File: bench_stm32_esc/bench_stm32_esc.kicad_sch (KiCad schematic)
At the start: 107 parts, among them CN1 S6B-PH-K-S-, CN10 Conn_02x19_Odd_Even, CN7 Conn_02x19_Odd_Even, J1 XT60PW-M, Q1 CSD19532Q5B, Q2 CSD19532Q5B, Q3 CSD19532Q5B, Q4 CSD19532Q5B, Q5 CSD19532Q5B, Q6 CSD19532Q5B, U1 DRV8353RSRGZT, U2 AMS1117, U3 TPD1E05U06DYA, U4 MR60PW-M.G.B, U7 TB60

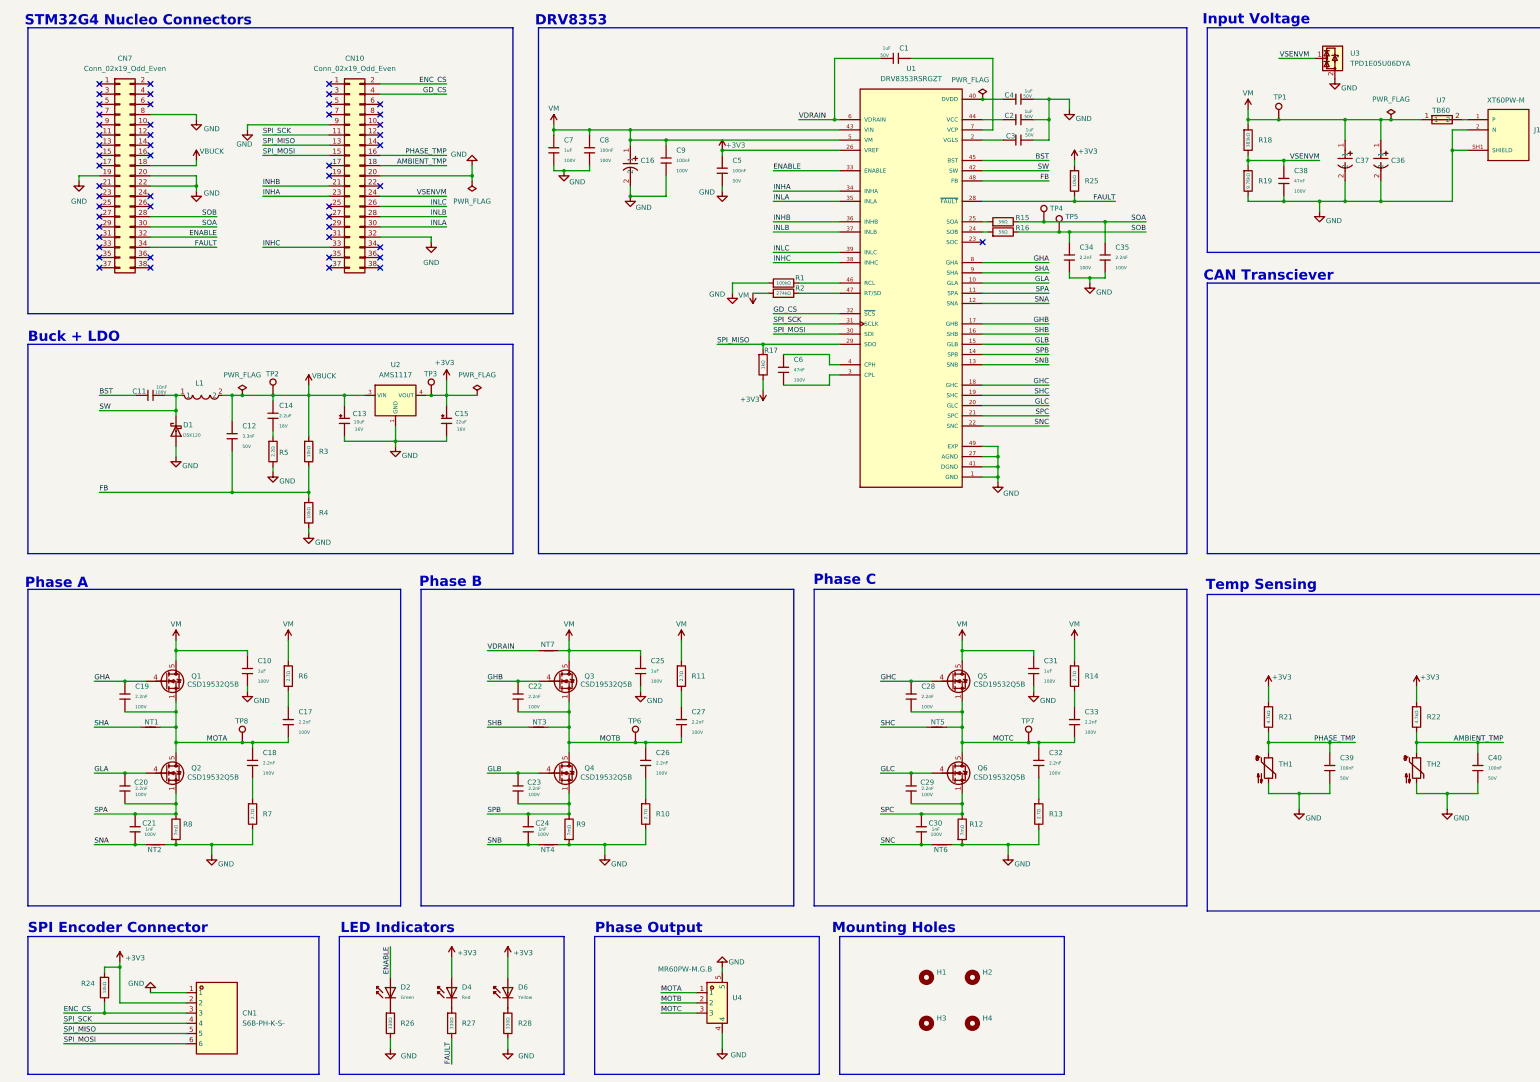
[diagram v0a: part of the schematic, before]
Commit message: Added smd stm32
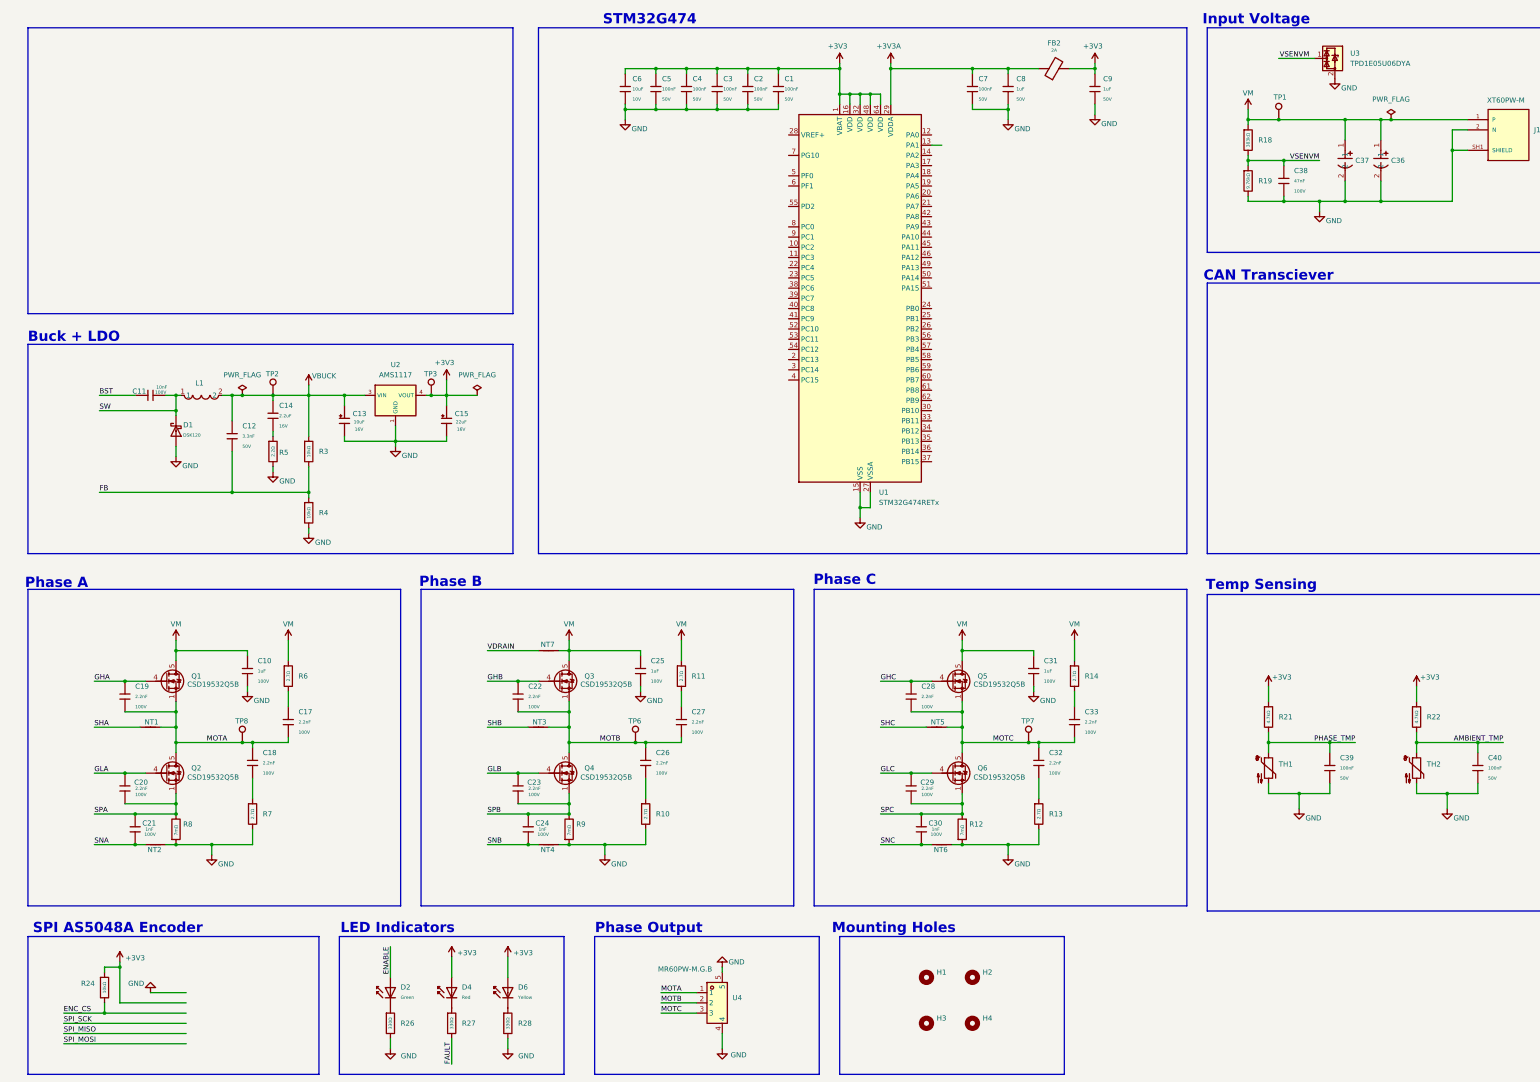
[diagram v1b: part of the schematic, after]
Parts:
- removed C1, C2, C3, C4: 1uF, PCM_JLCPCB:C_0603, symbol PCM_JLCPCB-Capacitors:0603,1uF
- removed C16: VT10UF100V167RV0127, footprints:VT10UF100V167RV0127, symbol VT10UF100V167RV0127:VT10UF100V167RV0127
- removed C34, C35: 2.2nF, PCM_JLCPCB:C_0603, symbol PCM_JLCPCB-Capacitors:0603,2.2uF
- removed C6: 47nF, PCM_JLCPCB:C_0603, symbol PCM_JLCPCB-Capacitors:0603,47nF
- removed C7: 1uF, PCM_JLCPCB:C_0805, symbol PCM_JLCPCB-Capacitors:0805,1uF
- removed C8, C9: 100nF, PCM_JLCPCB:C_0603, symbol PCM_JLCPCB-Capacitors:0603,100nF
- removed CN1: S6B-PH-K-S-, footprints:S6B-PH-K-S(LF)(SN), symbol S6B-PH-K-S(LF)(SN):S6B-PH-K-S-
- removed CN10, CN7: Conn_02x19_Odd_Even, Connector_PinSocket_2.54mm:PinSocket_2x19_P2.54mm_Vertical, symbol Connector_Generic:Conn_02x19_Odd_Even
- removed R1: 100kΩ, PCM_JLCPCB:R_0603, symbol PCM_JLCPCB-Resistors:0603,100kΩ
- removed R15, R16: 56Ω, PCM_JLCPCB:R_0603, symbol PCM_JLCPCB-Resistors:0603,56Ω
- removed R17: 1kΩ, PCM_JLCPCB:R_0603, symbol PCM_JLCPCB-Resistors:0603,1kΩ
- removed R2: 274kΩ, PCM_JLCPCB:R_0603, symbol PCM_JLCPCB-Resistors:0603,100kΩ
- removed R25: 10kΩ, PCM_JLCPCB:R_0603, symbol PCM_JLCPCB-Resistors:0603,10kΩ
- removed TP4, TP5: TestPoint, TestPoint:TestPoint_Pad_1.5x1.5mm, symbol Connector:TestPoint
- removed U1: DRV8353RSRGZT, footprints:QFN50P700X700X100-49N, symbol DRV8353RSRGZT:DRV8353RSRGZT
- removed U7: TB60, footprints:TB60, symbol TB60:TB60
- added C1, C2, C3, C4, C7: 100nF, PCM_JLCPCB:C_0603, symbol PCM_JLCPCB-Capacitors:0603,100nF
- added C6: 10uF, PCM_JLCPCB:C_0603, symbol PCM_JLCPCB-Capacitors:0603,10uF
- added C8, C9: 1uF, PCM_JLCPCB:C_0603, symbol PCM_JLCPCB-Capacitors:0603,1uF
- added FB2: (no value), PCM_JLCPCB:FB_0603, symbol PCM_JLCPCB-Inductors:Ferrite,0603,(2)
- added U1: STM32G474RETx, Package_QFP:LQFP-64_10x10mm_P0.5mm, symbol MCU_ST_STM32G4:STM32G474RETx
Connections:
- net +3V3: now also C1.1, C2.1, C3.1, C4.1, C6.2, C9.1, FB2.2, U1.1 (VBAT), U1.16 (VDD), U1.32 (VDD), U1.48 (VDD), U1.64 (VDD)
- net GND: now also C1.2, C2.2, C3.2, C4.2, C6.1, C7.2, C8.2, C9.2, U1.15 (VSS), U1.27 (VSSA), U1.31 (VSS), U1.47 (VSS), U1.63 (VSS)
- net VM: now also J1.1 (P)
- new net +3V3A: C7.1, C8.1, FB2.1, U1.29 (VDDA)
- no-connect marks 51 -> 0
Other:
- note added: "SPI AS5048A Encoder"
- note added: "STM32G474"
- note removed: "DRV8353"
- note removed: "SPI Encoder Connector"
- note removed: "STM32G4 Nucleo Connectors"

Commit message: New gate drivers
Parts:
- removed C11: 10nF, PCM_JLCPCB:C_0603, symbol PCM_JLCPCB-Capacitors:0603,100nF
- removed C12: 3.3nF, PCM_JLCPCB:C_0603, symbol PCM_JLCPCB-Capacitors:0603,3.3nF
- removed C13: 10uF, PCM_JLCPCB:C_CASE-A-3216-18(mm), symbol PCM_JLCPCB-Capacitors:CASE-A-3216-18(mm),10uF
- removed C14: 2.2uF, PCM_JLCPCB:C_0603, symbol PCM_JLCPCB-Capacitors:0603,2.2uF
- removed C15: 22uF, PCM_JLCPCB:C_CASE-A-3216-18(mm), symbol PCM_JLCPCB-Capacitors:CASE-A-3216-18(mm),10uF
- removed C17, C18, C22, C23, C26, C27, C28, C29, C32, C33: 2.2nF, PCM_JLCPCB:C_0603, symbol PCM_JLCPCB-Capacitors:0603,2.2uF
- removed C21, C24, C30: 1nF, PCM_JLCPCB:C_0603, symbol PCM_JLCPCB-Capacitors:0603,1nF
- removed C25, C31: 1uF, PCM_JLCPCB:C_0805, symbol PCM_JLCPCB-Capacitors:0805,1uF
- removed D1: DSK120, PCM_JLCPCB:D_SOD-123FL, symbol PCM_JLCPCB-Diodes:Schottky,DSK120
- removed D4: Red, PCM_JLCPCB:D_0805, symbol PCM_JLCPCB-Diodes:LED,0805,Red
- removed H4: MountingHole, MountingHole:MountingHole_3.2mm_M3, symbol Mechanical:MountingHole
- removed L1: SMDRH104R-331MT, footprints:SMDRH104R-331MT, symbol SMDRH104R-331MT:SMDRH104R-331MT
- removed NT1, NT2, NT3, NT4, NT5, NT6: NetTie_2, NetTie:NetTie-2_SMD_Pad0.5mm, symbol Device:NetTie_2
- removed NT7: NetTie_2, NetTie:NetTie-2_SMD_Pad2.0mm, symbol Device:NetTie_2
- removed Q3, Q4, Q5, Q6: CSD19532Q5B, Package_TO_SOT_SMD:TDSON-8-1, symbol Transistor_FET:CSD19532Q5B
- removed R10, R11, R13, R14, R6, R7: 2.7Ω, PCM_JLCPCB:R_0805, symbol PCM_JLCPCB-Resistors:0805,2.2Ω
- removed R12, R8, R9: 7mΩ, Resistor_SMD:R_2512_6332Metric, symbol Device:R
- removed R24, R3, R4: 10kΩ, PCM_JLCPCB:R_0603, symbol PCM_JLCPCB-Resistors:0603,10kΩ
- removed R27: 330Ω, PCM_JLCPCB:R_0603, symbol PCM_JLCPCB-Resistors:0603,330Ω
- removed R5: 2.2Ω, PCM_JLCPCB:R_0603, symbol PCM_JLCPCB-Resistors:0603,2.2Ω
- removed TP2, TP3, TP6, TP7: TestPoint, TestPoint:TestPoint_Pad_1.5x1.5mm, symbol Connector:TestPoint
- removed U2: AMS1117, PCM_JLCPCB:SOT-223-3_L6.5-W3.4-P2.30-LS7.0-BR, symbol PCM_JLCPCB-Power:LDO, 3.3V, 1A
- added C1, C4: 10pF, PCM_JLCPCB:C_0603, symbol PCM_JLCPCB-Capacitors:0603,10pF
- added C11, C12: 2.2nF, PCM_JLCPCB:C_0603, symbol PCM_JLCPCB-Capacitors:0603,2.2uF
- added C13, C19, C23, C28, C3, C5: 100nF, PCM_JLCPCB:C_0603, symbol PCM_JLCPCB-Capacitors:0603,100nF
- added C2, C25, C37, C42: 2.2uF, PCM_JLCPCB:C_0603, symbol PCM_JLCPCB-Capacitors:0603,2.2uF
- added C26, C6: 1uF, PCM_JLCPCB:C_0603, symbol PCM_JLCPCB-Capacitors:0603,1uF
- added C31, C36: 2.2nF, PCM_JLCPCB:C_0603, symbol PCM_JLCPCB-Capacitors:0603,2.2nF
- added C34: 58pF, PCM_JLCPCB:C_0603, symbol PCM_JLCPCB-Capacitors:0603,33pF
- added C39, C41, C44: 22uF, PCM_JLCPCB:C_0603, symbol PCM_JLCPCB-Capacitors:0603,22uF
- added FB1: (no value), PCM_JLCPCB:FB_0603, symbol PCM_JLCPCB-Inductors:Ferrite,0603
- added J1: USB_C_Receptacle_USB2.0_16P, Connector_USB:USB_C_Receptacle_HRO_TYPE-C-31-M-12, symbol Connector:USB_C_Receptacle_USB2.0_16P
- added L2: SM7850-680MT, footprints:SM7850-680MT, symbol SM7850-680MT:SM7850-680MT
- added R1, R3: 3.3Ω, PCM_JLCPCB:R_0603, symbol PCM_JLCPCB-Resistors:0603,4.7Ω
- added R10: 100kΩ, PCM_JLCPCB:R_0603, symbol PCM_JLCPCB-Resistors:0603,100kΩ
- added R13, R6: 10kΩ, PCM_JLCPCB:R_0603, symbol PCM_JLCPCB-Resistors:0603,10kΩ
- added R15: 150kΩ, PCM_JLCPCB:R_0603, symbol PCM_JLCPCB-Resistors:0603,150kΩ
- added R16, R17: 5.1kΩ, PCM_JLCPCB:R_0603, symbol PCM_JLCPCB-Resistors:0603,5.1kΩ
- added R19: 360kΩ, PCM_JLCPCB:R_0603, symbol PCM_JLCPCB-Resistors:0603,360kΩ
- added R21: 470kΩ, PCM_JLCPCB:R_0603, symbol PCM_JLCPCB-Resistors:0603,470kΩ
- added R4, R5: 2.7Ω, PCM_JLCPCB:R_0805, symbol PCM_JLCPCB-Resistors:0805,2.2Ω
- added R8: 330kΩ, PCM_JLCPCB:R_0603, symbol PCM_JLCPCB-Resistors:0603,330kΩ
- added SW1: SW_SPDT, symbol Switch:SW_SPDT
- added U1: UCC27211ADRMR, easyeda2kicad:VSON-8_L4.0-W4.0-P0.80-TL-EP, symbol easyeda2kicad:UCC27211ADRMR
- added U10: AS5047D, Package_SO:TSSOP-14_4.4x5mm_P0.65mm, symbol Sensor_Magnetic:AS5047D
- added U11: USBLC6-2P6, Package_TO_SOT_SMD:SOT-666, symbol Power_Protection:USBLC6-2P6
- added U4: AP2112K-3.3, Package_TO_SOT_SMD:SOT-23-5, symbol Regulator_Linear:AP2112K-3.3
- added U5: INA240A2D, Package_SO:SOIC-8_3.9x4.9mm_P1.27mm, symbol Amplifier_Current:INA240A2D
- added U8: LM5164DDA, Package_SO:HSOP-8-1EP_3.9x4.9mm_P1.27mm_EP2.41x3.1mm_ThermalVias, symbol Regulator_Switching:LM5164DDA
- added X1: X322516MLB4SI, PCM_JLCPCB:OSC-SMD_4P-L3.2-W2.5-BL, symbol PCM_JLCPCB-Crystals:Crystal, 16MHz, 9pF
- renumbered C6 to C14, C5 to C15, C4 to C16, C3 to C17, C2 to C18, C1 to C20, C7 to C21, C8 to C22, C38 to C27, C37 to C29, C36 to C32, C39 to C45, C40 to C46, C19 to C7, C20 to C8, D2 to D1, D6 to D2, H3 to H2, H2 to H3, J1 to J2, R18 to R11, R19 to R12, R26 to R22, R28 to R23, R21 to R24, R22 to R25, TP8 to TP1, TP1 to TP2, U4 to U12, U1 to U6, U3 to U9
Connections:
- net AMBIENT_TMP is gone; now on net AMB_TMP: C46.1, R25.2, TH2.1
- net SPA is gone; now on net GND: C8.2, Q2.1 (S), Q2.2 (S), Q2.3 (S)
- net +3V3: now also C19.1, C23.1, C26.1, C28.1, FB1.2, R13.1, SW1.3 (C), U10.11 (VDD), U4.5 (VOUT), U5.3 (REF2), U5.6 (V+); no longer FB2.2
- net +3V3A: now also FB1.1; no longer FB2.1
- net GHA: now also R3.2
- net GLA: now also R1.1
- net GND: now also C1.2, C13.2, C19.2, C2.2, C23.2, C25.2, C26.2, C28.2, C3.2, C37.2, C39.2, C4.2, C41.2, C42.2, C44.2, C6.2, J1.A1 (GND), J1.A12 (GND), J1.B1 (GND), J1.B12 (GND), J1.SH (SHIELD), R10.2, R15.2, R16.1, R17.1, R5.2, R8.2, SW1.1 (A), U1.7 (VSS), U1.9 (EP), U10.13 (GND), U10.5 (TST), U11.2 (GND), U4.2 (GND), U5.2 (GND), U5.4 (GND), U5.7 (REF1), U8.1 (GND), U8.9 (EP), X1.2 (GND), X1.4 (GND)
- net MOTA: now also U5.8 (+); no longer C7.2, Q1.1 (S), Q1.2 (S), Q1.3 (S), Q2.5 (D), TP1.1
- net PHASE_TMP: now also U6.13 (PA1)
- net SPI_MISO: now also U6.53 (PC11)
- net SPI_MOSI: now also U6.52 (PC10)
- net SPI_SCK: now also U6.54 (PC12)
- net VM: now also C25.1, R4.1, U8.2 (VIN)
- net VSENVM: now also U6.12 (PA0)
- net AMB_TMP: now reaches U6.14 (PA2)
- net CSA: now reaches U6.17 (PA3)
- net CSA: now also U5.5
- net CSB: now reaches U6.21 (PA7)
- net CSC: now reaches U6.24 (PB0)
- net PWM_LA: now reaches U6.35 (PB13)
- net PWM_LA: now also U1.6 (LI)
- net PWM_LB: now reaches U6.36 (PB14)
- net PWM_LC: now reaches U6.37 (PB15)
- net PWM_HA: now reaches U6.42 (PA8)
- net PWM_HA: now also U1.5 (HI)
- net PWM_HB: now reaches U6.43 (PA9)
- net PWM_HC: now reaches U6.44 (PA10)
- net USB_D-: now reaches U6.45 (PA11)
- net USB_D-: now also U11.6 (I/O1)
- net USB_D+: now reaches U6.46 (PA12)
- net USB_D+: now also U11.4 (I/O1)
- net SWCLK: now reaches U6.49 (PA13)
- net HSE_IN: now reaches U6.5 (PF0)
- net HSE_IN: now also C1.1, C4.1, X1.1 (OSC), X1.3 (OSC)
- net CAN_TX: now reaches U6.50 (PA14)
- net CAN_TX: now also U6.57 (PB4)
- net CAN_RX: now reaches U6.56 (PB3)
- net HSE_OUT: now reaches U6.6 (PF1)
- net BOOT0: now reaches U6.61 (PB8)
- net BOOT0: now also R6.1
- net NRST: now reaches U6.7 (PG10)
- net NRST: now also C13.1
- new net: R13.2, U10.1 (~{CS})
- new net: R1.2, U1.8 (LO)
- new net: C34.1, C36.1, R19.2
- new net: C11.1, R4.2
- new net: C11.2, C12.1
- new net: C5.1, U1.4 (HS)
- new net: C5.2, U1.2 (HB)
- new net: J1.B5 (CC2), R16.2
- new net: C12.2, R5.1
- new net: J1.A7 (D-), J1.B7 (D-), U11.1 (I/O2)
- new net: J1.A6 (D+), J1.B6 (D+), U11.3 (I/O2)
- new net: J1.A5 (CC1), R17.2
- new net: R3.1, U1.3 (HO)
- new net: C31.2, U8.7 (BST)
- new net +12V_VM: C2.1, C3.1, C36.2, C39.1, C41.1, C44.1, L2.2, R21.2, U1.1 (VDD)
- new net +5V_USB: C42.1, C6.1, FB2.2, U4.1 (VIN), U4.3 (EN)
- new net EN_12V: R8.1, U8.3 (EN/UVLO)
- new net FB_12V: C34.2, R15.1, R21.1, U8.5 (FB)
- new net MP_A: C7.2, Q1.1 (S), Q1.2 (S), Q1.3 (S), Q2.5 (D), TP1.1, U5.1 (-)
- new net RON_12V: R10.1, U8.4 (RON)
- new net SW_12V: C31.1, L2.1, R19.1, U8.8 (SW)
- new net SW_BOOT0: R6.2, SW1.2 (B)
- new net USB_VBUS: C37.1, FB2.1, J1.A4 (VBUS), J1.A9 (VBUS), J1.B4 (VBUS), J1.B9 (VBUS), U11.5 (VBUS)
- no-connect marks 0 -> 38
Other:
- note added: "12V Buck*"
- note added: "Crystal"
- note added: "Power ORing + LDO"
- note added: "SPI AS5047P Encoder"
- note added: "USB-C Connector"
- note removed: "Buck + LDO"
- note removed: "Phase B"
- note removed: "Phase C"
- note removed: "SPI AS5048A Encoder"
- moved on the sheet: C10, C21, C22, C45, C46, C7, C8, D1, D2, H1, H2, H3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
